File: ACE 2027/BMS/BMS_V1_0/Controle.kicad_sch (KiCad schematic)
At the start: 9 parts, among them J205 RJ45, J206 RJ45

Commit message: Avancement général du schémas
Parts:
- removed C211: 4,7µF, Capacitor_SMD:C_0805_2012Metric_Pad1.18x1.45mm_HandSolder, symbol Device:C
- removed R214, R215, R216, R217: 0Ω, Resistor_SMD:R_0402_1005Metric_Pad0.72x0.64mm_HandSolder, symbol Device:R_US
- added C201, C208: 22μF, Capacitor_SMD:C_0805_2012Metric_Pad1.18x1.45mm_HandSolder, symbol Device:C
- added C202, C203, C204, C207, C210: 0.1μF, Capacitor_SMD:C_0805_2012Metric_Pad1.18x1.45mm_HandSolder, symbol Device:C
- added C205, C206: 12pF, Capacitor_SMD:C_0805_2012Metric_Pad1.18x1.45mm_HandSolder, symbol Device:C
- added C209: 47nF, Capacitor_SMD:C_0603_1608Metric_Pad1.08x0.95mm_HandSolder, symbol Device:C
- added D202: USBLC6-2SC6, BIMU:SOT23-6L, symbol BIMU_Custom:USBLC6-2SC6
- added D203: CONNECTED LED, LED_SMD:LED_0805_2012Metric_Pad1.15x1.40mm_HandSolder, symbol Device:LED
- added J203: UART_connector, Connector_PinSocket_2.54mm:PinSocket_1x04_P2.54mm_Vertical, symbol Connector_Generic:Conn_01x04
- added J204: USB_C_Receptacle_USB2.0_16P, Connector_USB:USB_C_Receptacle_GCT_USB4105-xx-A_16P_TopMnt_Horizontal, symbol Connector:USB_C_Receptacle_USB2.0_16P
- added R202, R203, R208, R209: 5.1KΩ, Resistor_SMD:R_0805_2012Metric_Pad1.20x1.40mm_HandSolder, symbol Device:R_US
- added R210, R211: 330Ω, Resistor_SMD:R_0805_2012Metric_Pad1.20x1.40mm_HandSolder, symbol Device:R_US
- added R212: 50Ω, Resistor_SMD:R_0805_2012Metric_Pad1.20x1.40mm_HandSolder, symbol Device:R_US
- added SW201, SW202: SW_Push, Button_Switch_SMD:SW_SPST_B3U-1000P, symbol Switch:SW_Push
- added TP201: TP_CAN_P, TestPoint:TestPoint_Pad_1.0x1.0mm, symbol Connector:TestPoint
- added TP202: TP_CAN_N, TestPoint:TestPoint_Pad_1.0x1.0mm, symbol Connector:TestPoint
- added U201: ESP32-S3, Package_DFN_QFN:QFN-56-1EP_7x7mm_P0.4mm_EP4x4mm, symbol MCU_Espressif:ESP32-S3
- added U202: SN65HVD232DR, Package_SO:SOIC-8_3.9x4.9mm_P1.27mm, symbol Motor_controller:SN65HVD232DR
- added Y201: ABM8-40.000MHZ-10-D1G-T, Crystal:Crystal_SMD_2016-4Pin_2.0x1.6mm, symbol Device:Crystal_GND24
- D204: value POWER LED -> ERROR LED; Digi-Key_PN 1516-QBLP631-IG5CT-ND -> 1516-QBLP631-R5-2897CT-ND
- R213: value 330Ω -> 50Ω; Digi-Key_PN 541-4168-1-ND -> 541-CRCW080550R0FKTACT-ND
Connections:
- net I2C_SCL is gone; now on net GND: J205.4, J206.4
- net I2C_SDA is gone; now on net GND: J205.3, J206.3
- net +5V: now also J205.5, J205.6, J206.5, J206.6, C202.1, D202.5, J203.4 (Pin_4), J204.A4 (VBUS), J204.A9 (VBUS), J204.B4 (VBUS), J204.B9 (VBUS)
- net CAN_N: now also R213.2, TP202.1, U202.6 (CANL)
- net CAN_P: now also R212.1, TP201.1, U202.7 (CANH)
- net GND: now also D204.1 (K), C201.2, C202.2, C203.2, C204.2, C205.2, C206.2, C207.2, C208.2, C209.1, C210.2, D202.2, D203.1 (K), J203.1 (Pin_1), J204.A1 (GND), J204.A12 (GND), J204.B1 (GND), J204.B12 (GND), J204.S1 (SHIELD), R202.2, R203.2, SW201.1, SW202.1, U201.57 (GND), U202.2 (GND), Y201.2, Y201.4
- net U0RX: now also J203.2 (Pin_2), U201.50 (U0RXD)
- net U0TX: now also J203.3 (Pin_3), U201.49 (U0TXD)
- net at D204.2 (A): now also R211.1
- net at R213.1: now also C209.2, R212.2
- new net: D203.2 (A), R210.1
- new net: J204.A5 (CC1), R202.1
- new net: J204.B5 (CC2), R203.1
- new net: U201.55 (VDDA), U201.56 (VDDA)
- new net: D202.3, J204.A6 (D+), J204.B6 (D+)
- new net: D202.1, J204.A7 (D-), J204.B7 (D-)
- new net +3.3V: C201.1, C207.1, C208.1, C210.1, R208.2, R209.2, U201.2 (VDD3P3), U201.3 (VDD3P3), U202.3 (VCC)
- new net BOOT: C204.1, R208.1, SW202.2
- new net CONNECTED LED: R210.2
- new net EN: C203.1, R209.1, SW201.2
- new net ERROR_LED: R211.2
- new net TWAI_CAN_RX: U202.4 (RXD)
- new net TWAI_CAN_TX: U202.1 (TXD)
- new net USB_D+: D202.4, U201.26 (GPIO20/USB_D+)
- new net USB_D-: D202.6, U201.25 (GPIO19/USB_D-)
- new net XTAL_N: C206.1, U201.53 (XTAL_N), Y201.3
- new net XTAL_P: C205.1, U201.54 (XTAL_P), Y201.1
- no-connect marks 0 -> 2
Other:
- note added: "CAN"
- note added: "CONNECTORS"
- note added: "Clock 40MHZ ±10PPM pour le ESP-32"
- note added: "ESP-32 CLOCK"
- note added: "ESP32-S3"
- note added: "LEDS AND BUTTONS"

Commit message: Amélioration de la présentation
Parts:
- J203: renamed from J205; value RJ45 -> MoBo
- J204: renamed from J206; value RJ45 -> BIMU
- renumbered C210 to C202, C202 to C203, C203 to C204, C204 to C205, C205 to C206, C206 to C207, C207 to C208, C208 to C209, C209 to C210, D202 to D201, D203 to D202, D204 to D203, J203 to J201, J204 to J202, R202 to R201, R203 to R202, R208 to R203, R209 to R204, R210 to R205, R211 to R206, R212 to R207, R213 to R208
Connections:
- net +5V: no longer J204.5, J204.6
- net GND: no longer J204.3, J204.4
- no-connect marks 2 -> 6

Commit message: Avancement circuit sélecteur
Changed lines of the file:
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@@
 	(global_label "TWAI_CAN_TX"
 		(shape input)
-		(at 41.91 299.72 180)
-		(fields_autoplaced yes)
-		(effects
-			(font
-				(size 1.27 1.27)
-			)
-			(justify right)
-		)
-		(property "Intersheetrefs" "${INTERSHEET_REFS}"
-			(at 27.011 299.72 0)
-			(hide yes)
-			(show_name no)
-			(do_not_autoplace no)
-			(effects
-				(font
-					(size 1.27 1.27)
-				)
-				(justify right)
+		(at 198.12 314.96 180)
+		(fields_autoplaced yes)
+		(effects
+			(font
+				(size 1.27 1.27)
+			)
+			(justify right)
+		)
+		(property "Intersheetrefs" "${INTERSHEET_REFS}"
+			(at 183.221 314.96 0)
+			(hide yes)
+			(show_name no)
+			(do_not_autoplace no)
+			(effects
+				(font
+					(size 1.27 1.27)
+				)
+				(justify right)
+			)
+		)
+	)
+	(global_label "Voltage_Sense_Gauche"
+		(shape bidirectional)
+		(at 187.96 275.59 0)
+		(fields_autoplaced yes)
+		(effects
+			(font
+				(size 1.27 1.27)
+			)
+			(justify left)
+		)
+		(property "Intersheetrefs" "${INTERSHEET_REFS}"
+			(at 213.4648 275.59 0)
+			(hide yes)
+			(show_name no)
+			(do_not_autoplace no)
+			(effects
+				(font
+					(size 1.27 1.27)
+				)
+				(justify left)
+			)
+		)
+	)
+	(global_label "Current_Sense_Droite"
+		(shape bidirectional)
+		(at 191.77 284.48 0)
+		(fields_autoplaced yes)
+		(effects
+			(font
+				(size 1.27 1.27)
+			)
+			(justify left)
+		)
+		(property "Intersheetrefs" "${INTERSHEET_REFS}"
+			(at 215.9445 284.48 0)
+			(hide yes)
+			(show_name no)
+			(do_not_autoplace no)
+			(effects
+				(font
+					(size 1.27 1.27)
+				)
+				(justify left)
 			)
 		)
@@
 	(global_label "EN"
 		(shape bidirectional)
-		(at 41.91 292.1 180)
-		(fields_autoplaced yes)
-		(effects
-			(font
-				(size 1.27 1.27)
-			)
-			(justify right)
-		)
-		(property "Intersheetrefs" "${INTERSHEET_REFS}"
-			(at 35.334 292.1 0)
+		(at 198.12 307.34 180)
+		(fields_autoplaced yes)
+		(effects
+			(font
+				(size 1.27 1.27)
+			)
+			(justify right)
+		)
+		(property "Intersheetrefs" "${INTERSHEET_REFS}"
+			(at 191.544 307.34 0)
 			(hide yes)
 			(show_name no)
@@
 		)
 	)
+	(global_label "Current_Sense_Gauche"
+		(shape bidirectional)
+		(at 187.96 261.62 0)
+		(fields_autoplaced yes)
+		(effects
+			(font
+				(size 1.27 1.27)
+			)
+			(justify left)
+		)
+		(property "Intersheetrefs" "${INTERSHEET_REFS}"
+			(at 213.4044 261.62 0)
+			(hide yes)
+			(show_name no)
+			(do_not_autoplace no)
+			(effects
+				(font
+					(size 1.27 1.27)
+				)
+				(justify left)
+			)
+		)
+	)
 	(global_label "XTAL_N"
 		(shape input)
@@
 	(global_label "ERROR_LED"
 		(shape input)
-		(at 63.5 307.34 180)
-		(fields_autoplaced yes)
-		(effects
-			(font
-				(size 1.27 1.27)
-			)
-			(justify right)
-		)
-		(property "Intersheetrefs" "${INTERSHEET_REFS}"
-			(at 49.8106 307.34 0)
+		(at 195.58 321.31 180)
+		(fields_autoplaced yes)
+		(effects
+			(font
+				(size 1.27 1.27)
+			)
+			(justify right)
+		)
+		(property "Intersheetrefs" "${INTERSHEET_REFS}"
+			(at 181.8906 321.31 0)
 			(hide yes)
 			(show_name no)
@@
 	(global_label "TWAI_CAN_RX"
 		(shape input)
-		(at 41.91 297.18 180)
-		(fields_autoplaced yes)
-		(effects
-			(font
-				(size 1.27 1.27)
-			)
-			(justify right)
-		)
-		(property "Intersheetrefs" "${INTERSHEET_REFS}"
-			(at 26.7086 297.18 0)
+		(at 198.12 312.42 180)
+		(fields_autoplaced yes)
+		(effects
+			(font
+				(size 1.27 1.27)
+			)
+			(justify right)
+		)
+		(property "Intersheetrefs" "${INTERSHEET_REFS}"
+			(at 182.9186 312.42 0)
 			(hide yes)
 			(show_name no)
@@
 	(global_label "CONNECTED LED"
 		(shape input)
-		(at 64.77 306.07 0)
-		(fields_autoplaced yes)
-		(effects
-			(font
-				(size 1.27 1.27)
-			)
-			(justify left)
-		)
-		(property "Intersheetrefs" "${INTERSHEET_REFS}"
-			(at 83.237 306.07 0)
+		(at 196.85 320.04 0)
+		(fields_autoplaced yes)
+		(effects
+			(font
+				(size 1.27 1.27)
+			)
+			(justify left)
+		)
+		(property "Intersheetrefs" "${INTERSHEET_REFS}"
+			(at 215.317 320.04 0)
+			(hide yes)
+			(show_name no)
+			(do_not_autoplace no)
+			(effects
+				(font
+					(size 1.27 1.27)
+				)
+				(justify left)
+			)
+		)
+	)
+	(global_label "Voltage_Sense_Selecteur"
+		(shape bidirectional)
+		(at 186.69 297.18 0)
+		(fields_autoplaced yes)
+		(effects
+			(font
+				(size 1.27 1.27)
+			)
+			(justify left)
+		)
+		(property "Intersheetrefs" "${INTERSHEET_REFS}"
+			(at 214.1906 297.18 0)
+			(hide yes)
+			(show_name no)
+			(do_not_autoplace no)
+			(effects
+				(font
+					(size 1.27 1.27)
+				)
+				(justify left)
+			)
+		)
+	)
+	(global_label "Voltage_Sense_Droite"
+		(shape bidirectional)
+		(at 191.77 292.1 0)
+		(fields_autoplaced yes)
+		(effects
+			(font
+				(size 1.27 1.27)
+			)
+			(justify left)
+		)
+		(property "Intersheetrefs" "${INTERSHEET_REFS}"
+			(at 216.0049 292.1 0)
 			(hide yes)
 			(show_name no)
@@
 	(global_label "BOOT"
 		(shape bidirectional)
-		(at 71.12 302.26 0)
-		(fields_autoplaced yes)
-		(effects
-			(font
-				(size 1.27 1.27)
-			)
-			(justify left)
-		)
-		(property "Intersheetrefs" "${INTERSHEET_REFS}"
-			(at 80.1151 302.26 0)
-			(hide yes)
-			(show_name no)
+		(at 203.2 316.23 0)
+		(fields_autoplaced yes)
+		(effects
+			(font
+				(size 1.27 1.27)
+			)
+			(justify left)
+		)
+		(property "Intersheetrefs" "${INTERSHEET_REFS}"
+			(at 212.1951 316.23 0)
+			(hide yes)
+			(show_name no)

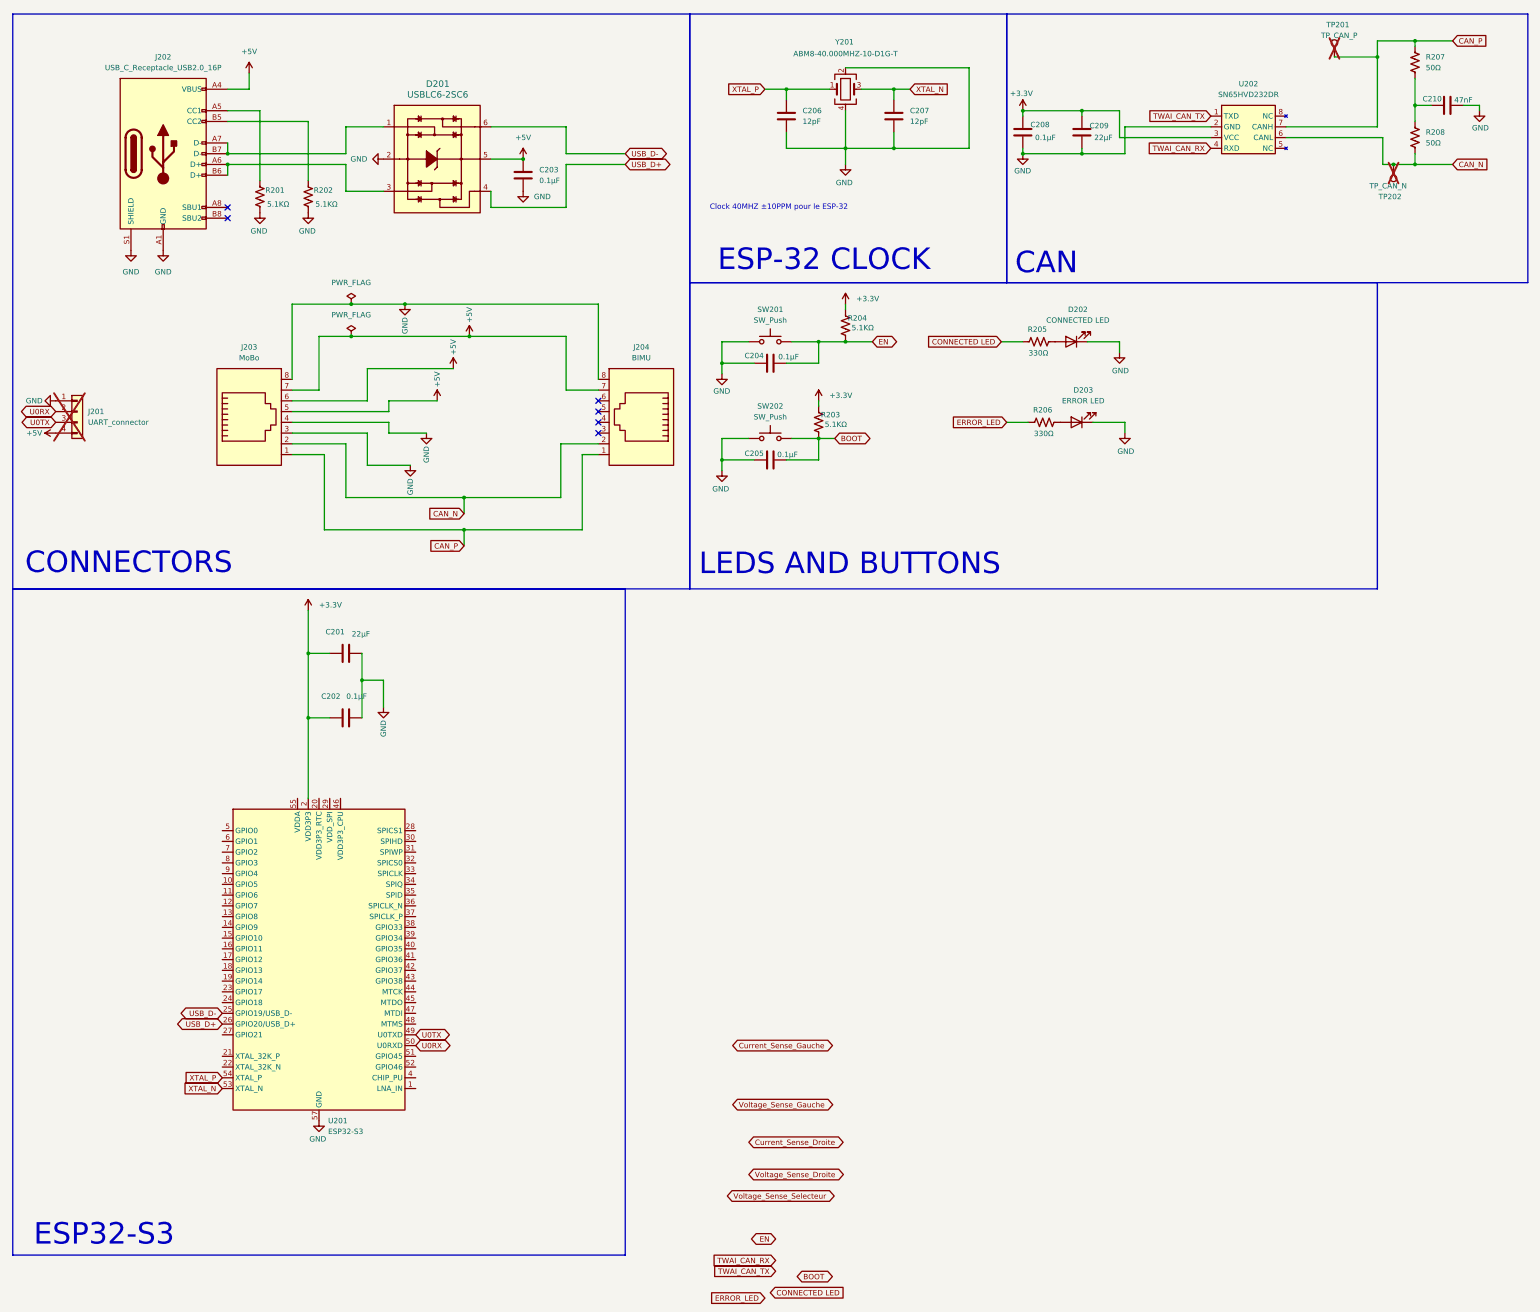
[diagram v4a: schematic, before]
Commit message: Avancement circuit pour les LED
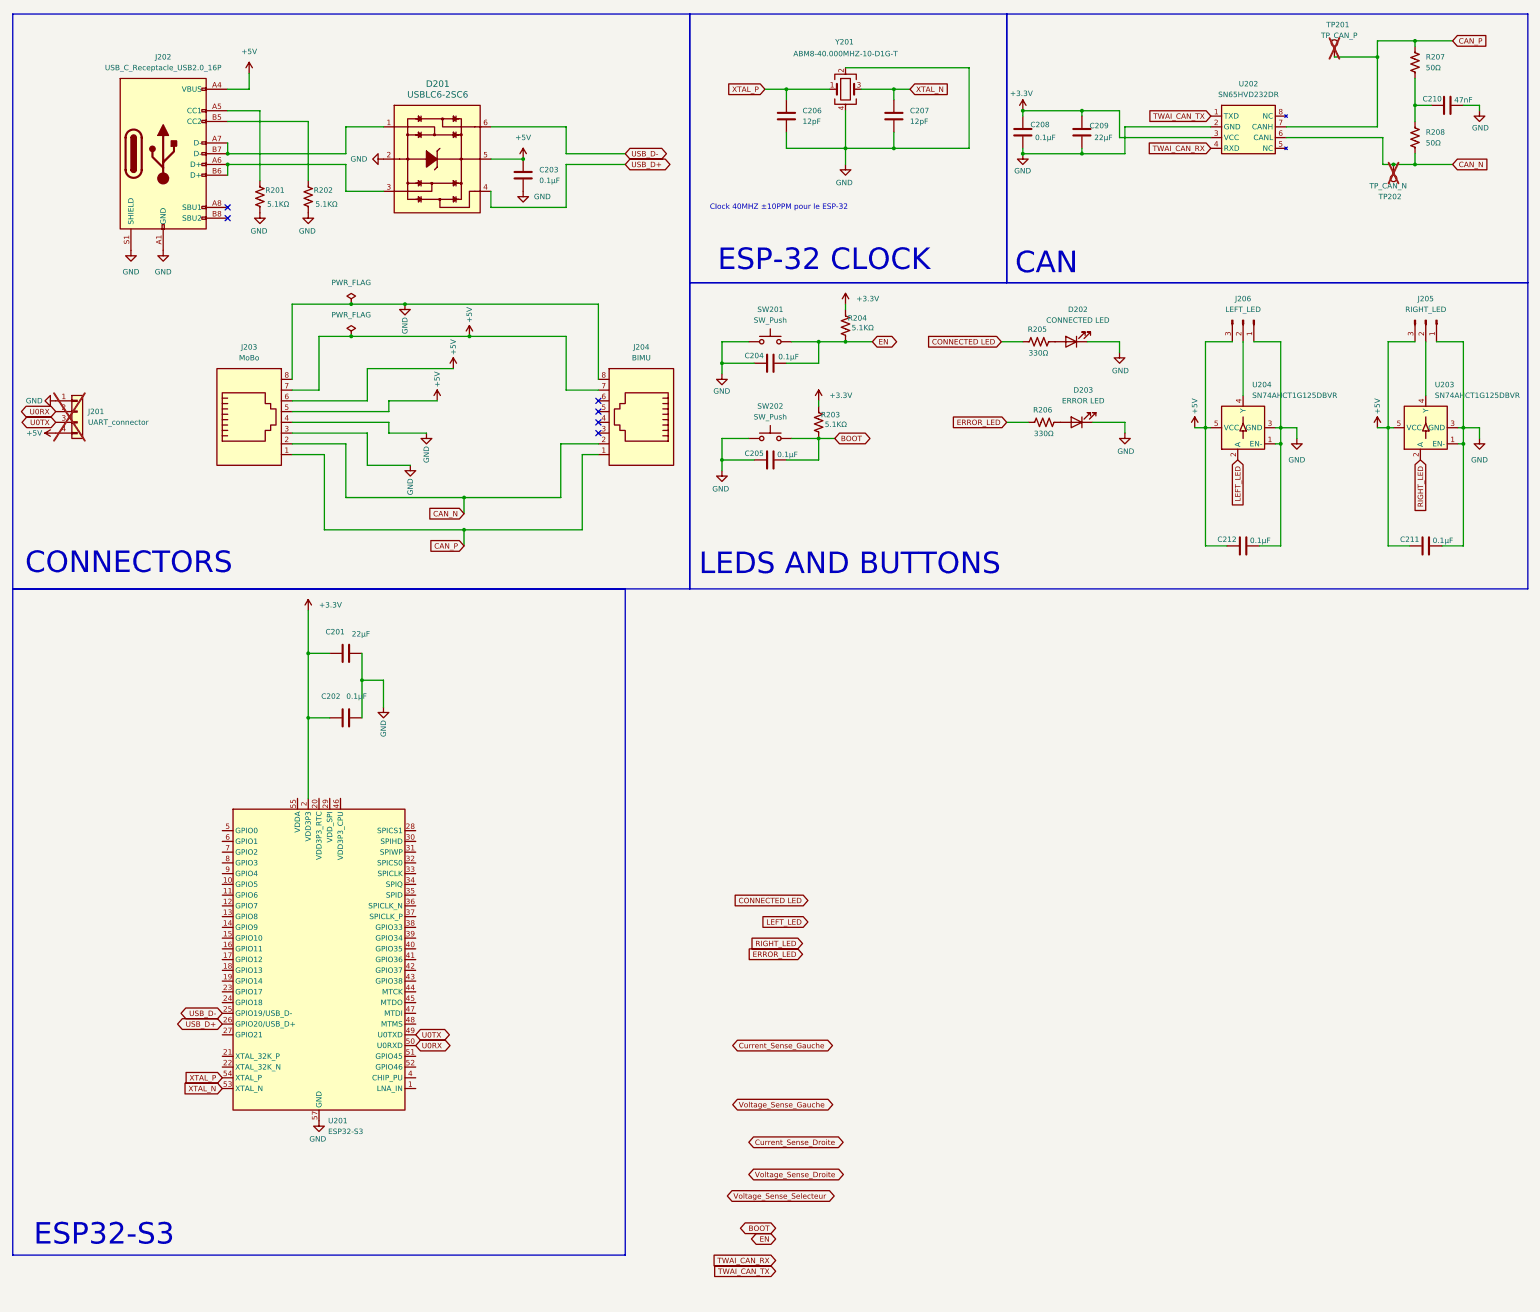
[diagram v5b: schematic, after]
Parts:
- added C211, C212: 0.1μF, Capacitor_SMD:C_0805_2012Metric_Pad1.18x1.45mm_HandSolder, symbol Device:C
- added J205: RIGHT_LED, Connector_JST:JST_XH_B3B-XH-A_1x03_P2.50mm_Vertical, symbol Connector:Conn_01x03_Pin
- added J206: LEFT_LED, Connector_JST:JST_XH_B3B-XH-A_1x03_P2.50mm_Vertical, symbol Connector:Conn_01x03_Pin
- added U203, U204: SN74AHCT1G125DBVR, Package_TO_SOT_SMD:SOT-23-5, symbol BMS:Level_shifter
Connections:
- net +5V: now also C211.2, C212.2, J205.3 (Pin_3), J206.3 (Pin_3), U203.5 (VCC), U204.5 (VCC)
- net GND: now also C211.1, C212.1, J205.1 (Pin_1), J206.1 (Pin_1), U203.1 (EN-), U203.3 (GND), U204.1 (EN-), U204.3 (GND)
- new net: J205.2 (Pin_2), U203.4 (Y)
- new net: J206.2 (Pin_2), U204.4 (Y)
- new net LEFT_LED: U204.2 (A)
- new net RIGHT_LED: U203.2 (A)

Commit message: Fixer l'erreur des bimu
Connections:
- net +3.3V: now also U201.20 (VDD3P3_RTC), U201.29 (VDD_SPI), U201.46 (VDD3P3_CPU), U201.55 (VDDA), U201.56 (VDDA)
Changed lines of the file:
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@@
+	)
+	(junction
+		(at 87.63 203.2)
+		(diameter 0)
+		(color 0 0 0 0)
 	)
 	(junction
@@
 	)
 	(junction
+		(at 92.71 203.2)
+		(diameter 0)
+		(color 0 0 0 0)
+	)
+	(junction
 		(at 97.79 93.98)
 		(diameter 0)
@@
 	(junction
 		(at 185.42 123.19)
+		(diameter 0)
+		(color 0 0 0 0)
+	)
+	(junction
+		(at 90.17 203.2)
 		(diameter 0)
 		(color 0 0 0 0)
@@
 	(wire
 		(pts
+			(xy 92.71 203.2) (xy 95.25 203.2)
+		)
+		(stroke
+			(width 0)
+			(type default)
+		)
+	)
+	(wire
+		(pts
 			(xy 364.49 40.64) (xy 364.49 39.37)
 		)
@@
 	(wire
 		(pts
+			(xy 90.17 203.2) (xy 92.71 203.2)
+		)
+		(stroke
+			(width 0)
+			(type default)
+		)
+	)
+	(wire
+		(pts
 			(xy 270.51 50.8) (xy 280.67 50.8)
 		)
@@
 	(wire
 		(pts
+			(xy 85.09 203.2) (xy 87.63 203.2)
+		)
+		(stroke
+			(width 0)
+			(type default)
+		)
+	)
+	(wire
+		(pts
 			(xy 360.68 115.57) (xy 360.68 119.38)
 		)
 		(stroke
+			(width 0)
+			(type default)
+		)
+	)
+	(wire
+		(pts
+			(xy 87.63 203.2) (xy 90.17 203.2)
+		)
+		(stroke
